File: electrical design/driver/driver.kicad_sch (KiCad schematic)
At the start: 18 parts, among them J1 Conn_01x02_Female, J2 Conn_01x06_Female, J3 Conn_01x07_Male, Q1 IRFR5410PbF, U1 VNH5050A-E

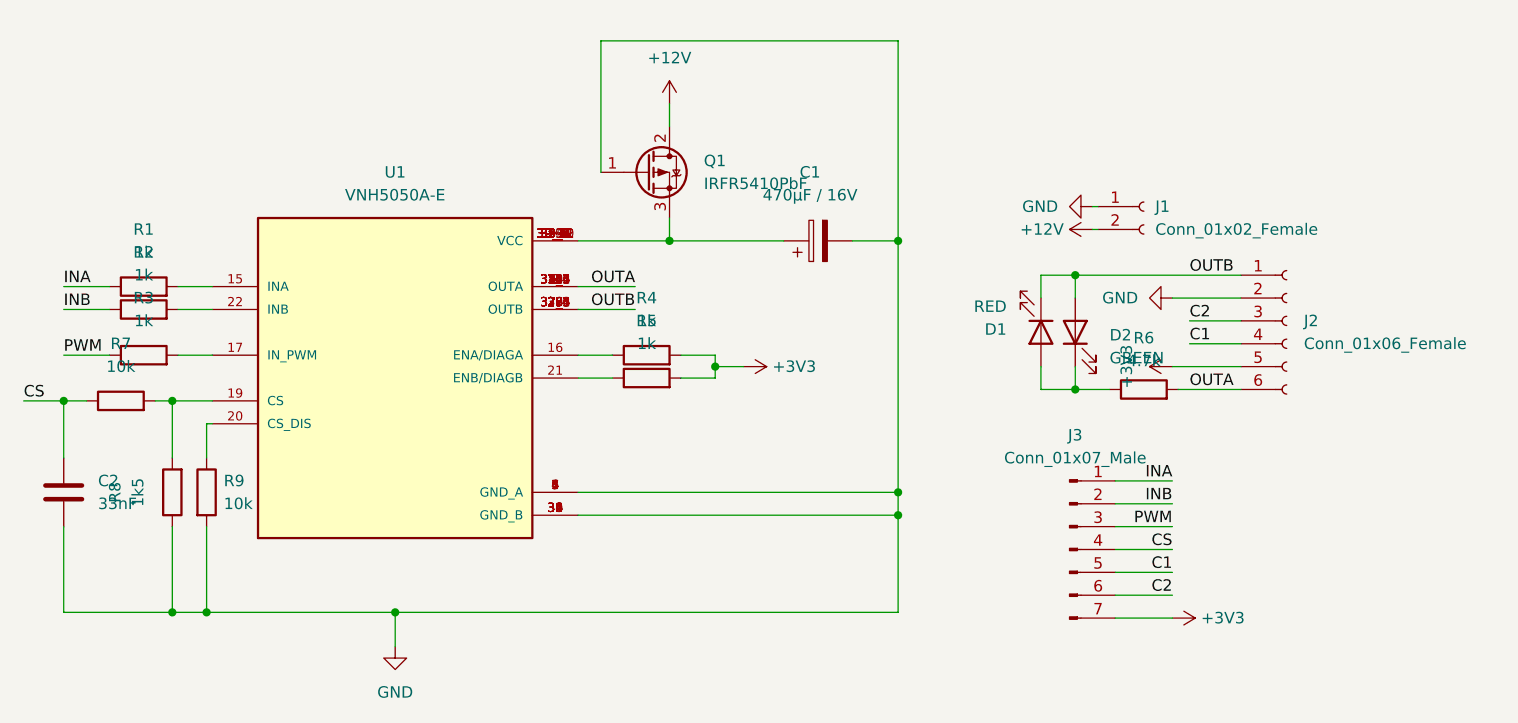
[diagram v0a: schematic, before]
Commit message: finish finalised VNH5050A breakout board
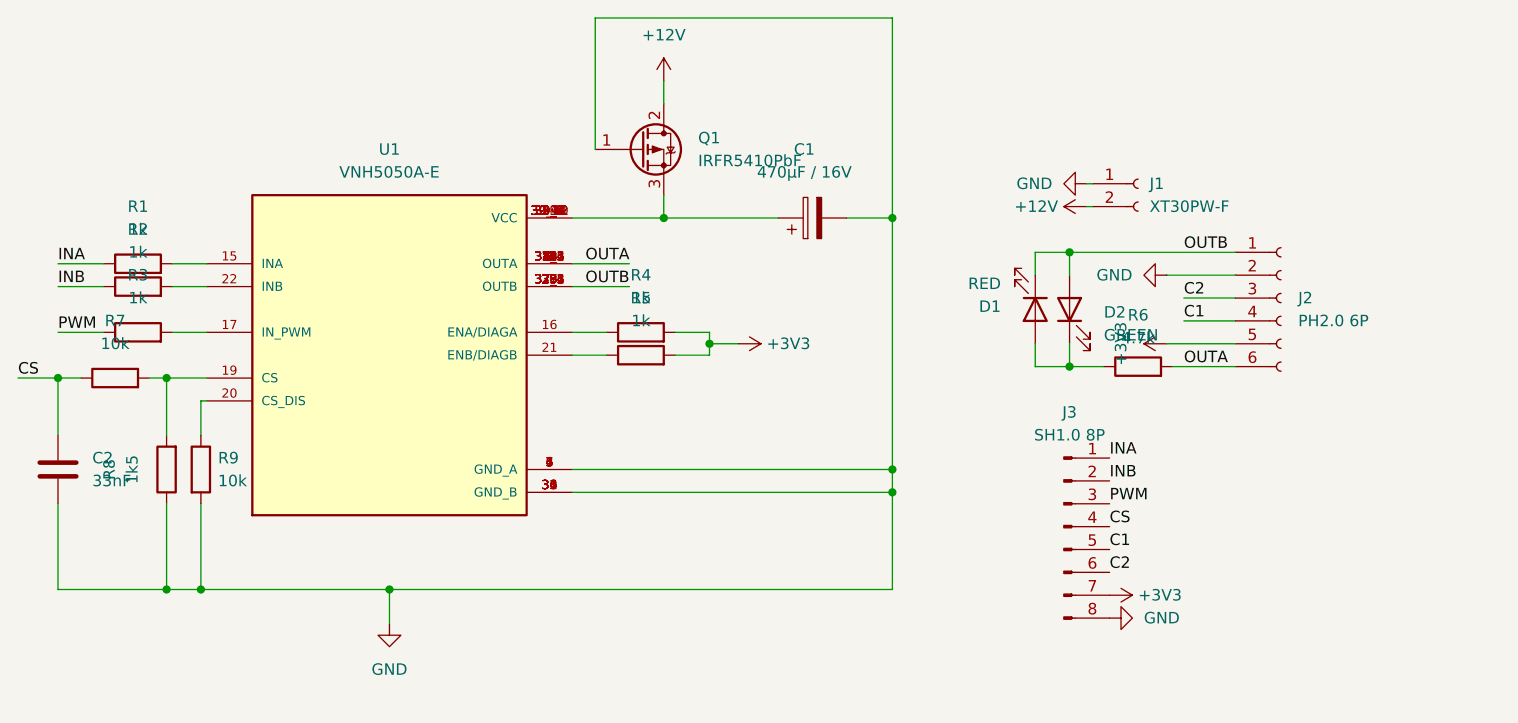
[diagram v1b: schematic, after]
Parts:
- removed J3: Conn_01x07_Male, Connectors:1X07_LOCK, symbol Connector:Conn_01x07_Male
- added J3: SH1.0 8P, Connector_JST:JST_SH_BM08B-SRSS-TB_1x08-1MP_P1.00mm_Vertical, symbol Connector:Conn_01x08_Male
- J1: value Conn_01x02_Female -> XT30PW-F; footprint Connector_AMASS:AMASS_XT30UPB-F_1x02_P5.0mm_Vertical -> Connector_AMASS:AMASS_XT30PW-F_1x02_P2.50mm_Horizontal
- J2: value Conn_01x06_Female -> PH2.0 6P
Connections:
- net +3V3: now also J3.7 (Pin_7)
- net C1: now also J3.5 (Pin_5)
- net C2: now also J3.6 (Pin_6)
- net CS: now also J3.4 (Pin_4)
- net GND: now also J3.8 (Pin_8)
- net INA: now also J3.1 (Pin_1)
- net INB: now also J3.2 (Pin_2)
- net PWM: now also J3.3 (Pin_3)
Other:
- company: (none) -> 8076 Robotics
- title: (none) -> VNH5050A breakout board schematic drawing
